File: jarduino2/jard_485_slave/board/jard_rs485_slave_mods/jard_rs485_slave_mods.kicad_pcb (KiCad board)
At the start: 2 copper layers, 90 x 85 mm, 27 parts, among them J1 NETWORK IN, J2 NETWORK OUT, J3 LED, J4 LED, J5 Debit, J6 Niveau, J7 Electrovanne 12V, Q1 BPC_2N2222A, Q2 P03P4L-04, U1 BPC_Mod485, U2 BPC_DHT22

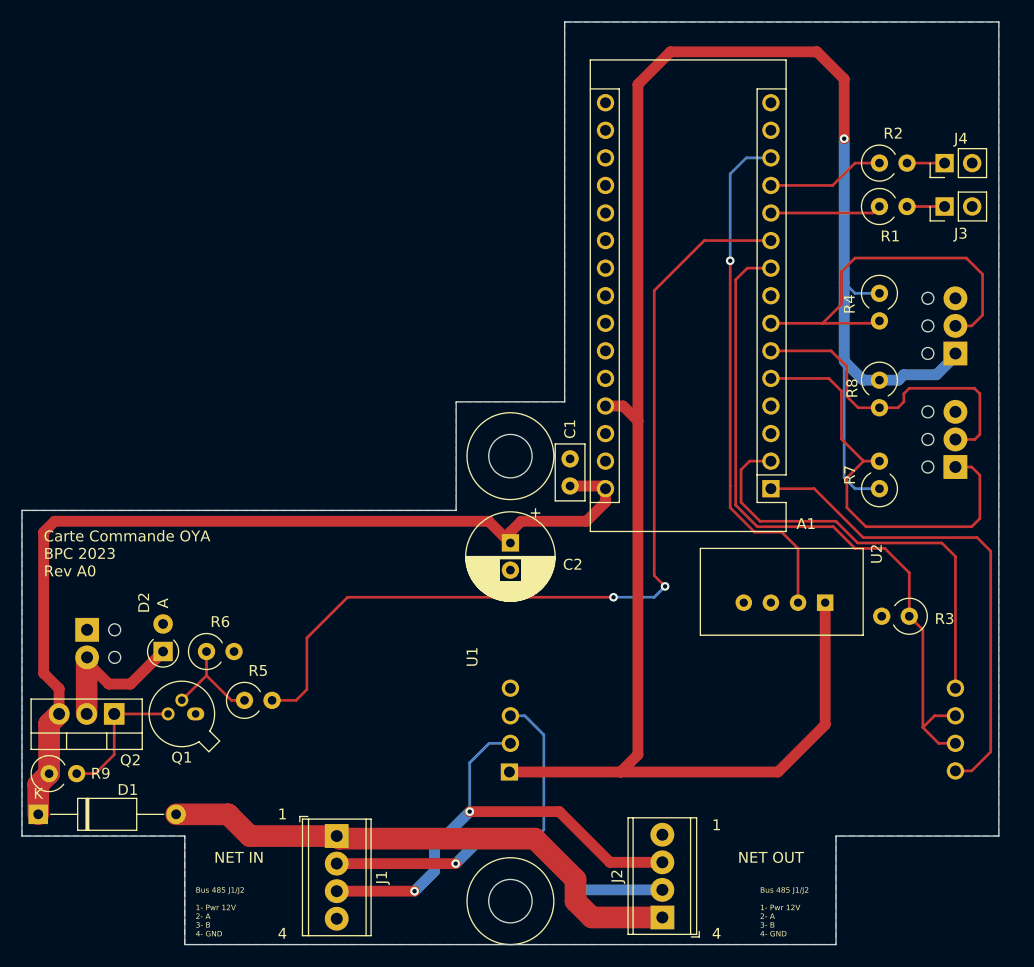
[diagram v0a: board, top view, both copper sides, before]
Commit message: Ajout AO de mesure de courant + mesure de tension
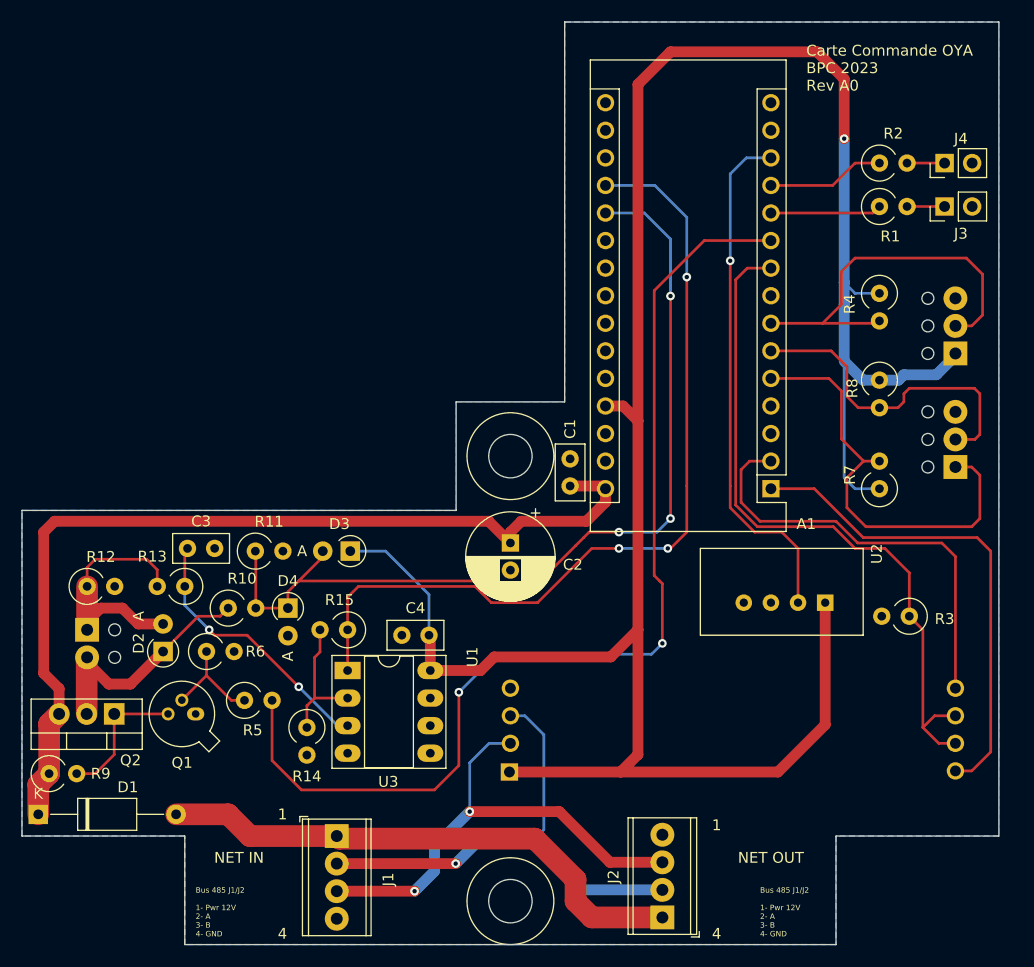
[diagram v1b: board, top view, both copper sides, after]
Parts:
- added C3: 100n, Capacitor_THT:C_Disc_D5.0mm_W2.5mm_P2.50mm, F.Cu at (118.8, 93.5)
- added C4: 100n, Capacitor_THT:C_Disc_D5.0mm_W2.5mm_P2.50mm, F.Cu at (136.0, 101.5)
- added D3: D, Diode_THT:D_A-405_P2.54mm_Vertical_AnodeUp, F.Cu at (131.2, 93.8)
- added D4: D, Diode_THT:D_A-405_P2.54mm_Vertical_AnodeUp, F.Cu at (125.5, 99.0)
- added R10: 100k, Resistor_THT:R_Axial_DIN0309_L9.0mm_D3.2mm_P2.54mm_Vertical, F.Cu at (120.0, 99.0)
- added R11: 40k, Resistor_THT:R_Axial_DIN0309_L9.0mm_D3.2mm_P2.54mm_Vertical, F.Cu at (122.5, 93.8)
- added R12: 30mR, Resistor_THT:R_Axial_DIN0309_L9.0mm_D3.2mm_P2.54mm_Vertical, F.Cu at (107.0, 97.0)
- added R13: 10k, Resistor_THT:R_Axial_DIN0309_L9.0mm_D3.2mm_P2.54mm_Vertical, F.Cu at (116.0, 97.0)
- added R14: 1k, Resistor_THT:R_Axial_DIN0309_L9.0mm_D3.2mm_P2.54mm_Vertical, F.Cu at (127.2, 110.0)
- added R15: 32k, Resistor_THT:R_Axial_DIN0309_L9.0mm_D3.2mm_P2.54mm_Vertical, F.Cu at (131.0, 101.0)
- added U3: LM358, Package_DIP:DIP-8_W7.62mm_Socket_LongPads, F.Cu at (131.0, 104.8)
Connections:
- A1 pad 19: Net-(A1-Pad19) -> MES_I
- A1 pad 20: Net-(A1-Pad20) -> MES_V
- D2 pad 2: GND -> Net-(D2-Pad2)
- J7 pad 1: GND -> Net-(D2-Pad2)
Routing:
- net MES_V: track 0.00 -> 85.2 mm, vias 0 -> 3
- net MES_I: track 0.00 -> 79.5 mm, vias 0 -> 3
- net Vcc: track 187.4 -> 224.1 mm
- net Net-(C3-Pad2): track 0.00 -> 24.9 mm, vias 0 -> 2
- net Net-(D2-Pad2): track 0.00 -> 22.6 mm
- net CMD_EV: track 83.7 -> 97.6 mm
- net Net-(R14-Pad1): track 0.00 -> 12.5 mm
- net Net-(D2-Pad1): track 14.4 -> 22.0 mm
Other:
- board text added: "12V/5A"
- board text removed: "12V"

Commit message: Amélioration suite protos
- Aggrandissement sérigraphie brochages
- Correction inversion sérigraphie 1 et 4 de J2
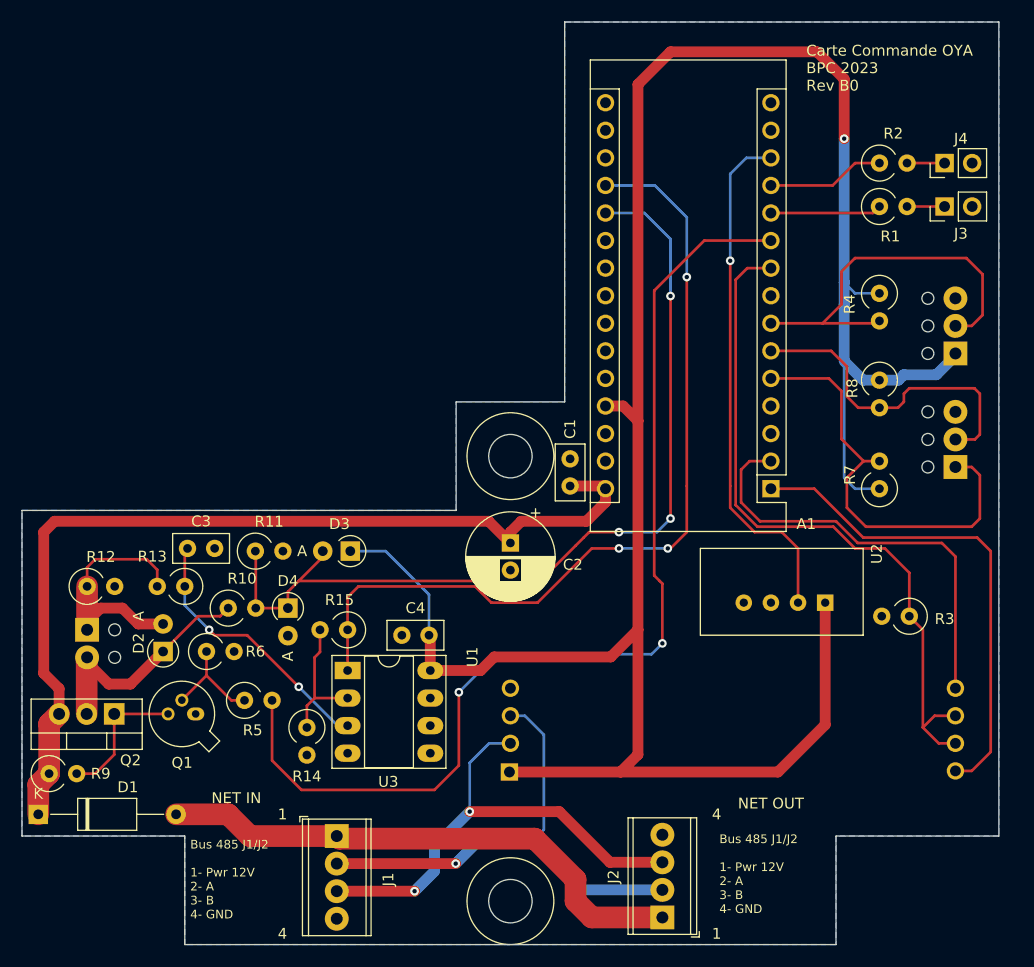
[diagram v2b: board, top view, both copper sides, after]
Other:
- board text added: "Carte Commande OYA BPC 2023 Rev B0"
- board text removed: "Carte Commande OYA BPC 2023 Rev A0"

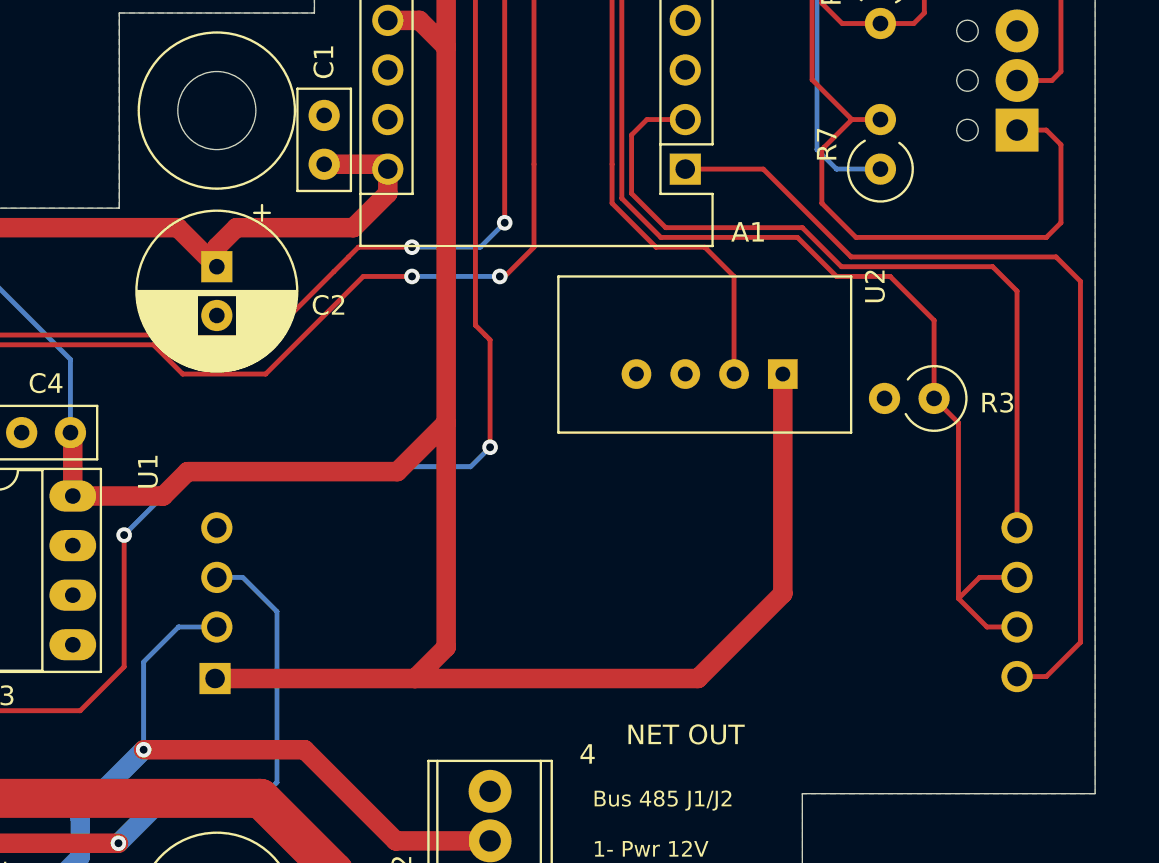
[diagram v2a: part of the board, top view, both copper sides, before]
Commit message: Correction inversion RX/TX
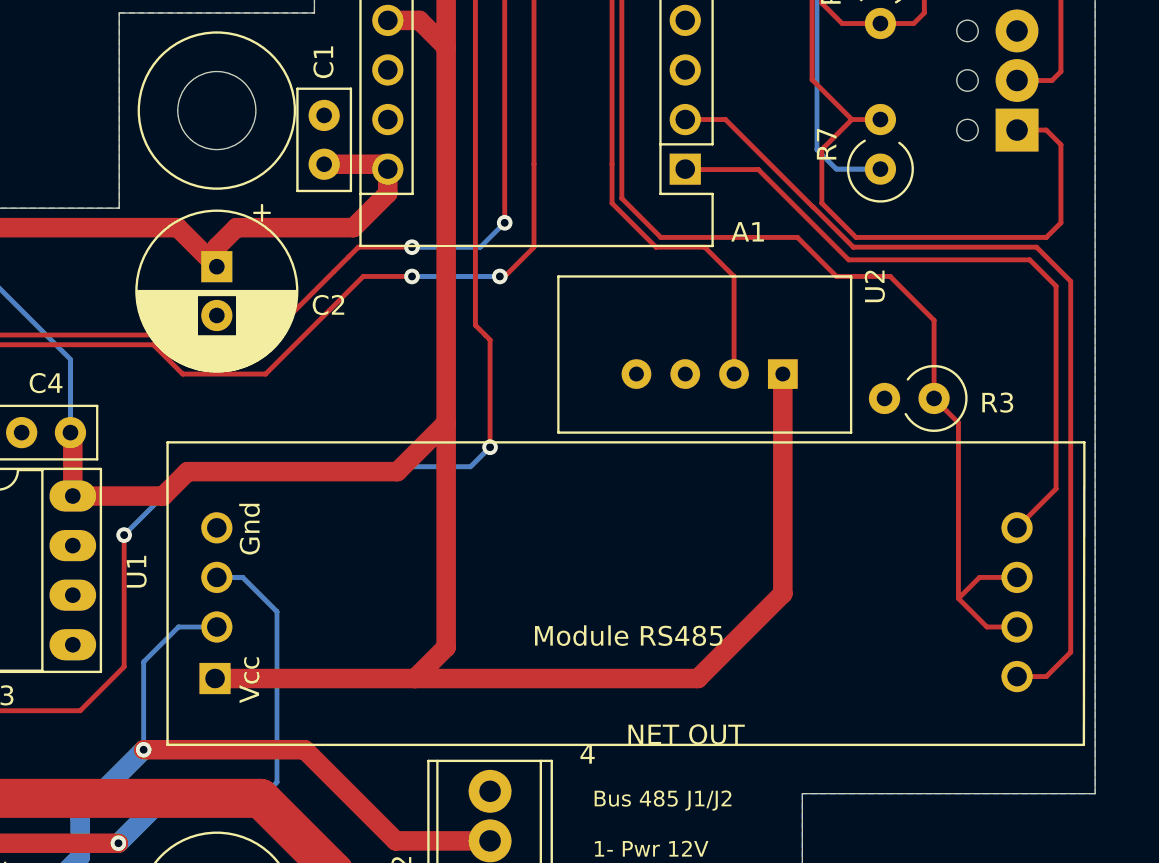
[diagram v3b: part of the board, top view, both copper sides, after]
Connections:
- U1 pad 5: RX -> TX
- U1 pad 8: TX -> RX
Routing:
- net TX: track 45.1 -> 34.7 mm
- net RX: track 40.0 -> 45.5 mm

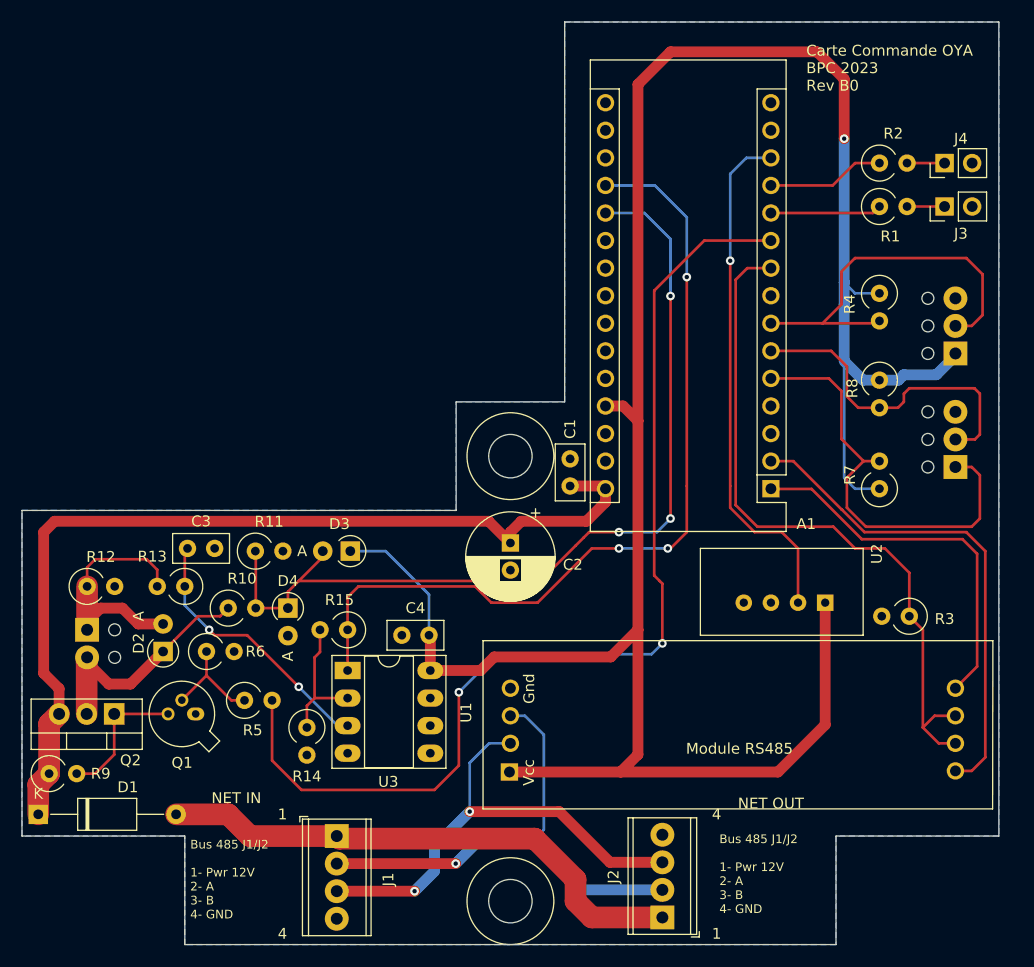
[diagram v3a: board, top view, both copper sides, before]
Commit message: Agrandir sérigraphie connecteurs bus Correction erreur inversion sérigraphie 1 et 4 sur J2 Correction inversion RX/TX sur module RS485 Inversion sérigraphie Niveaux/Débit
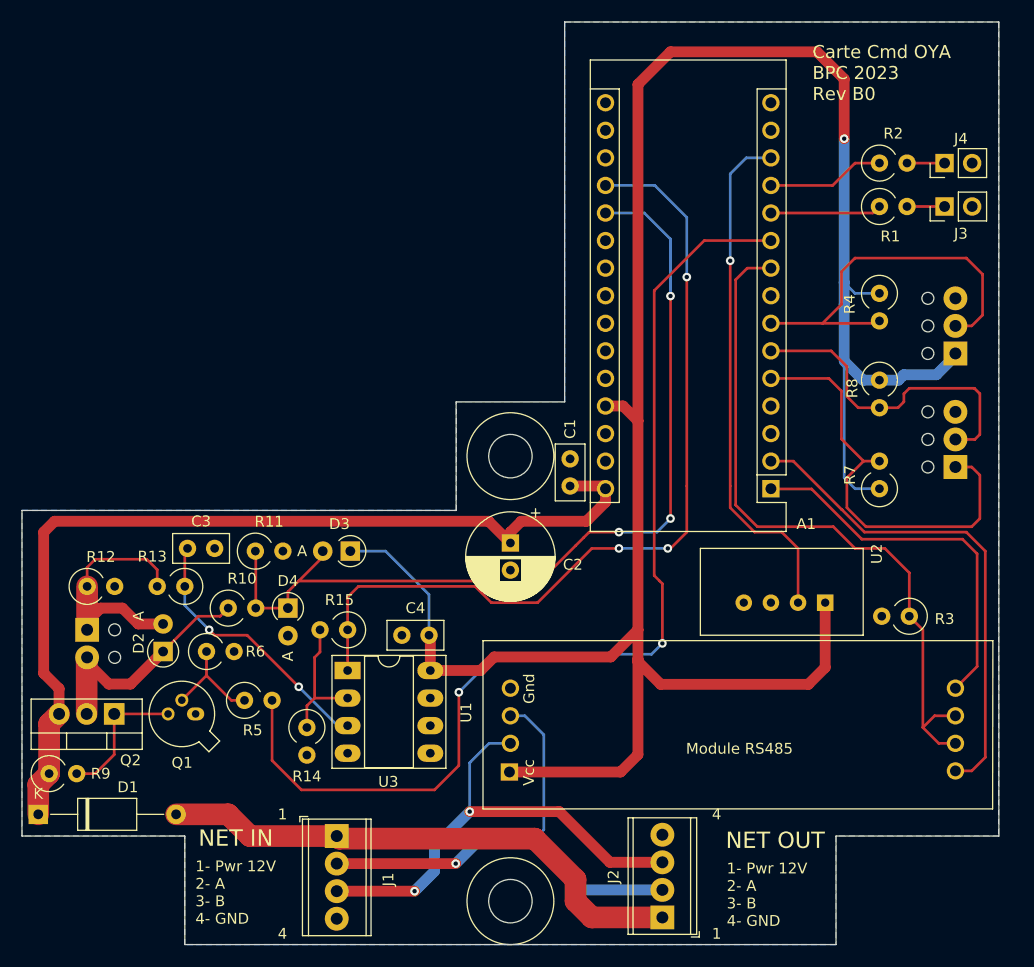
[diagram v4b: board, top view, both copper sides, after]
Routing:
- net Vcc: track 224.1 -> 217.1 mm
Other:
- board text added: "1- Pwr 12V 2- A 3- B 4- GND"
- board text added: "Carte Cmd OYA BPC 2023 Rev B0"
- board text added: "J6: Niveaux 1- Bas 2- Haut 3- Gnd"
- board text removed: "Bus 485 J1/J2 1- Pwr 12V 2- A 3- B 4- GND"
- board text removed: "Carte Commande OYA BPC 2023 Rev B0"
- board text removed: "J5: Niveaux 1- Bas 2- Haut 3- Gnd"
